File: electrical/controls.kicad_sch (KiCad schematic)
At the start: 0 parts

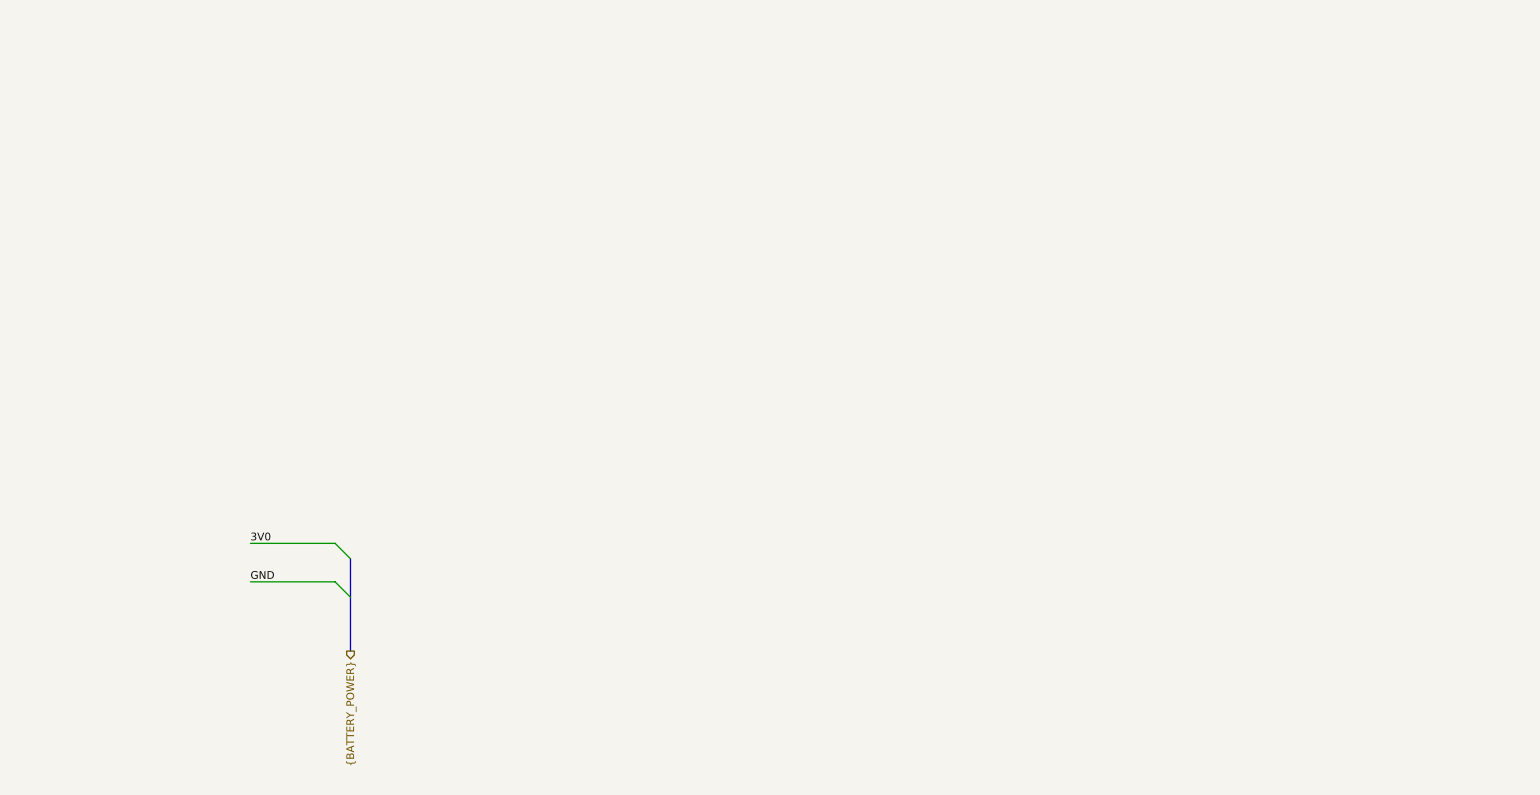
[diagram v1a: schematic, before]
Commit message: #3 Implementing potentionometers and  beginning IOC file creation.
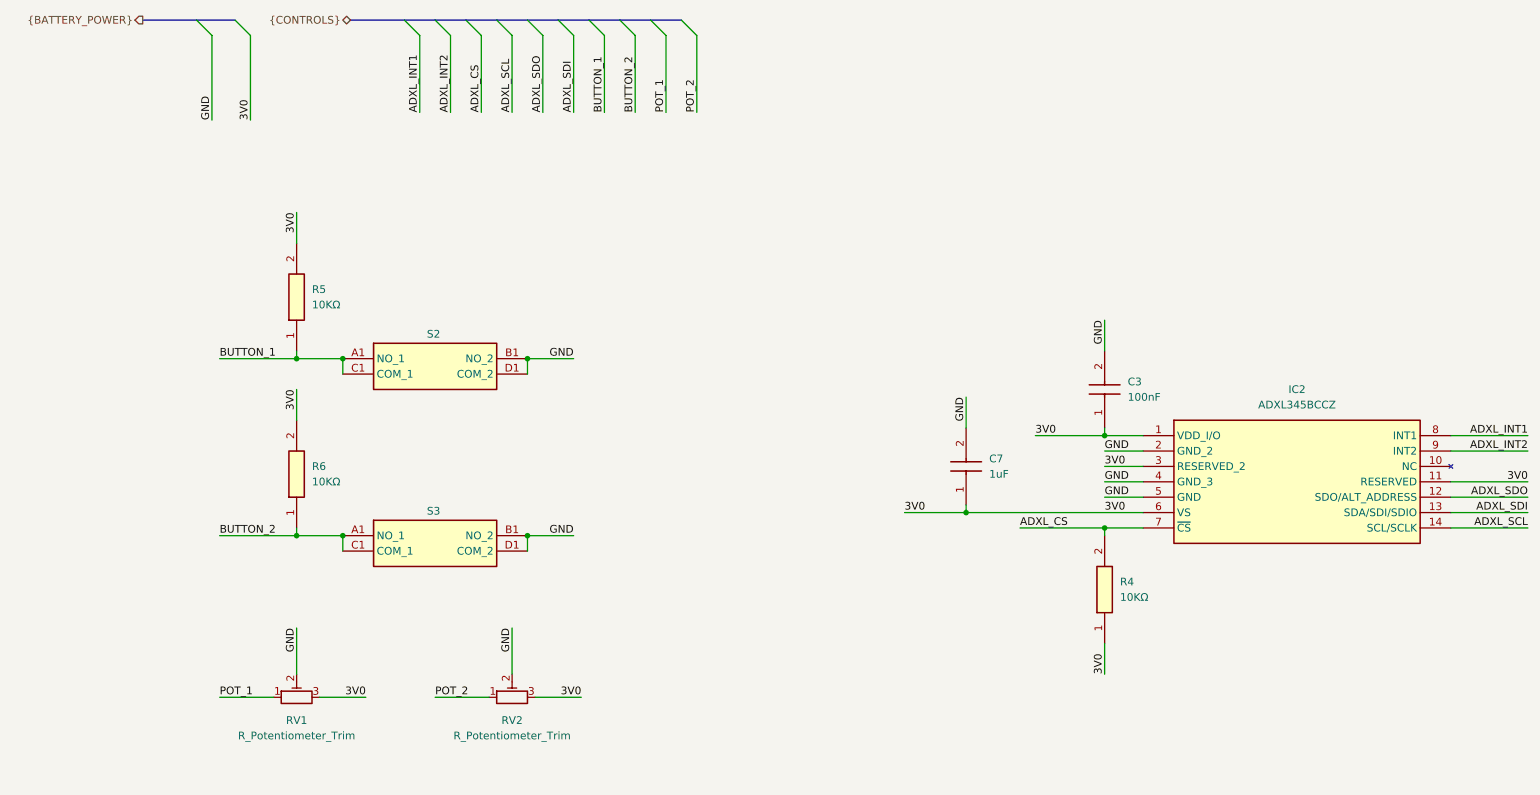
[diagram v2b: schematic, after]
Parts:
- added C3: 100nF, SamacSys_Parts:MAJx16, symbol SamacSys_Parts:MAJCH168BB7104KTEA01
- added C7: 1uF, SamacSys_Parts:CAPC1709X100N, symbol SamacSys_Parts:TACL105K010FTA
- added IC2: ADXL345BCCZ, LGA14R80P3X6_300X500X100, symbol SamacSys_Parts:ADXL345BCCZ
- added R4, R5, R6: 10KΩ, SamacSys_Parts:RESC1608X58N, symbol SamacSys_Parts:RA73F1J10KBTDF
- added RV1, RV2: R_Potentiometer_Trim, custom:potentiometer, symbol Device:R_Potentiometer_Trim
- added S2, S3: PTS125SM73SMTR21M_LFS, SamacSys_Parts:PTS125SM73SMTR21MLFS, symbol SamacSys_Parts:PTS125SM73SMTR21M_LFS
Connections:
- net 3V0: now also C3.1, C7.1, IC2.1 (VDD_I/O), IC2.11 (RESERVED), IC2.3 (RESERVED_2), IC2.6 (VS), R4.1, R5.2, R6.2, RV1.3, RV2.3
- net GND: now also C3.2, C7.2, IC2.2 (GND_2), IC2.4 (GND_3), IC2.5 (GND), RV1.2, RV2.2, S2.B1 (NO_2), S2.D1 (COM_2), S3.B1 (NO_2), S3.D1 (COM_2)
- new net ADXL_CS: IC2.7 (~{CS}), R4.2
- new net ADXL_INT1: IC2.8 (INT1)
- new net ADXL_INT2: IC2.9 (INT2)
- new net ADXL_SCL: IC2.14 (SCL/SCLK)
- new net ADXL_SDI: IC2.13 (SDA/SDI/SDIO)
- new net ADXL_SDO: IC2.12 (SDO/ALT_ADDRESS)
- new net BUTTON_1: R5.1, S2.A1 (NO_1), S2.C1 (COM_1)
- new net BUTTON_2: R6.1, S3.A1 (NO_1), S3.C1 (COM_1)
- new net POT_1: RV1.1
- new net POT_2: RV2.1
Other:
- title: (none) -> Etchasketch - Controls

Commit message: #3 Adding controls connections to STM32, updating IOC file to match.
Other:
- company: (none) -> AlumaPower
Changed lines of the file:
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@@
 		(title "Etchasketch - Controls")
 		(rev "1")
+		(company "AlumaPower")
 	)
 	(junction

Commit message: not in working state yet.
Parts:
- removed R6: 10KΩ, SamacSys_Parts:RESC1608X58N, symbol SamacSys_Parts:RA73F1J10KBTDF
- added R2: 10KΩ, SamacSys_Parts:RESC1608X58N, symbol SamacSys_Parts:RA73F1J10KBTDF
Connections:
- net 3V0: now also R5.1, R2.1; no longer R5.2
- net BUTTON_1: now also R5.2, S2.B1 (NO_2); no longer R5.1, S2.C1 (COM_1)
- net BUTTON_2: now also S3.B1 (NO_2), R2.2; no longer S3.C1 (COM_1)
- net GND: now also S2.C1 (COM_1), S3.C1 (COM_1); no longer S2.B1 (NO_2), S3.B1 (NO_2)
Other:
- moved on the sheet: R5, RV1, RV2, S2

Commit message: #17 Making layout. Errors rpesent.
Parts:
- IC2: footprint LGA14R80P3X6_300X500X100 -> SamacSys_Parts:LGA14R80P3X6_300X500X100
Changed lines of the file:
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@@
 		(company "AlumaPower")
+	)
+	(bus_alias "CONTROLS"
+		(members "ADXL_INT1" "ADXL_INT2" "ADXL_CS" "ADXL_SCL" "ADXL_SDO" "ADXL_SDI"
+			"BUTTON_1" "BUTTON_2" "POT_1" "POT_2"
+		)
 	)
 	(junction
@@
 			)
 		)
-		(property "Footprint" "LGA14R80P3X6_300X500X100"
+		(property "Footprint" "SamacSys_Parts:LGA14R80P3X6_300X500X100"
 			(at 250.19 186.36 0)
 			(effects
